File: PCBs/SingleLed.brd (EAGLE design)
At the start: 11.1 x 29.2 mm, 4 parts

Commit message: Updated
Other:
- board size 11.1 x 29.2 mm -> 15 x 28.7 mm
- board text added: "PinwheelRobotics"
- board text added: "care@pinwheel.in"
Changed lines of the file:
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@@
 <setting verticaltext="up"/>
 </settings>
-<grid distance="50" unitdist="mil" unit="mm" style="lines" multiple="1" display="yes" altdistance="5" altunitdist="mil" altunit="mm"/>
+<grid distance="0.5" unitdist="mm" unit="mm" style="lines" multiple="1" display="yes" altdistance="5" altunitdist="mil" altunit="mm"/>
 <layers>
 <layer number="1" name="Top" color="4" fill="1" visible="yes" active="yes"/>
@@
 <layer number="43" name="vRestrict" color="2" fill="10" visible="yes" active="yes"/>
 <layer number="44" name="Drills" color="7" fill="1" visible="no" active="yes"/>
-<layer number="45" name="Holes" color="7" fill="1" visible="no" active="yes"/>
+<layer number="45" name="Holes" color="7" fill="1" visible="yes" active="yes"/>
 <layer number="46" name="Milling" color="3" fill="1" visible="no" active="yes"/>
 <layer number="47" name="Measures" color="7" fill="1" visible="no" active="yes"/>
@@
 <board>
 <plain>
-<wire x1="17.78" y1="13.97" x2="28.88" y2="13.97" width="0" layer="20"/>
-<wire x1="28.88" y1="13.97" x2="28.88" y2="43.17" width="0" layer="20"/>
-<wire x1="28.88" y1="43.17" x2="17.78" y2="43.17" width="0" layer="20"/>
-<wire x1="17.78" y1="43.17" x2="17.78" y2="13.97" width="0" layer="20"/>
+<wire x1="14.95735625" y1="41.5157875" x2="14.998034375" y2="14.995496875" width="0" layer="20"/>
+<wire x1="14.998034375" y1="14.995496875" x2="16.28164375" y2="13.714" width="0" layer="20" curve="89.911983"/>
+<wire x1="16.28164375" y1="13.714" x2="28.00465625" y2="13.714" width="0" layer="20"/>
+<wire x1="28.00465625" y1="13.714" x2="30" y2="15.70934375" width="0" layer="20" curve="90"/>
+<wire x1="30" y1="15.70934375" x2="30" y2="41.302534375" width="0" layer="20"/>
+<wire x1="30" y1="41.302534375" x2="28.902534375" y2="42.4" width="0" layer="20" curve="90"/>
+<wire x1="28.902534375" y1="42.4" x2="15.84123125" y2="42.4" width="0" layer="20"/>
+<wire x1="15.84123125" y1="42.4" x2="14.95735625" y2="41.5157875" width="0" layer="20" curve="90.021878"/>
+<hole x="17.018" y="40.386" drill="3"/>
+<hole x="17.018" y="16.002" drill="3"/>
+<hole x="27.94" y="16.002" drill="3"/>
+<hole x="27.94" y="40.513" drill="3"/>
+<text x="17.272" y="17.653" size="1.778" layer="21" rot="R90">PinwheelRobotics</text>
+<text x="29.718" y="37.465" size="1.778" layer="22" rot="MR270">care@pinwheel.in</text>
 </plain>
 <attributes>
@@
 </element>
 <element name="U$2" library="microbit" package="MICROBIT_PAD" value="MICROBIT_PAD" x="22.479" y="35.306" smashed="yes" rot="R180">
-<attribute name="NAME" x="26.035" y="41.529" size="1.27" layer="21" rot="R270"/>
+<attribute name="NAME" x="17.653" y="36.449" size="1.27" layer="21" rot="R270"/>
 </element>
 <element name="R1" library="adafruit" package="0204/7" value="" x="26.67" y="31.75" smashed="yes" rot="R270">

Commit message: New Update
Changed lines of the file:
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@@
 <drawing>
 <settings>
-<setting alwaysvectorfont="yes"/>
+<setting alwaysvectorfont="no"/>
 <setting verticaltext="up"/>
 </settings>
@@
 <wire x1="28.902534375" y1="42.4" x2="15.84123125" y2="42.4" width="0" layer="20"/>
 <wire x1="15.84123125" y1="42.4" x2="14.95735625" y2="41.5157875" width="0" layer="20" curve="90.021878"/>
-<hole x="17.018" y="40.386" drill="3"/>
-<hole x="17.018" y="16.002" drill="3"/>
-<hole x="27.94" y="16.002" drill="3"/>
-<hole x="27.94" y="40.513" drill="3"/>
+<hole x="17" y="40.5" drill="3"/>
+<hole x="17" y="16" drill="3"/>
+<hole x="28" y="16" drill="3"/>
+<hole x="28" y="40.5" drill="3"/>
 <text x="17.272" y="17.653" size="1.778" layer="21" rot="R90">PinwheelRobotics</text>
 <text x="29.718" y="37.465" size="1.778" layer="22" rot="MR270">care@pinwheel.in</text>

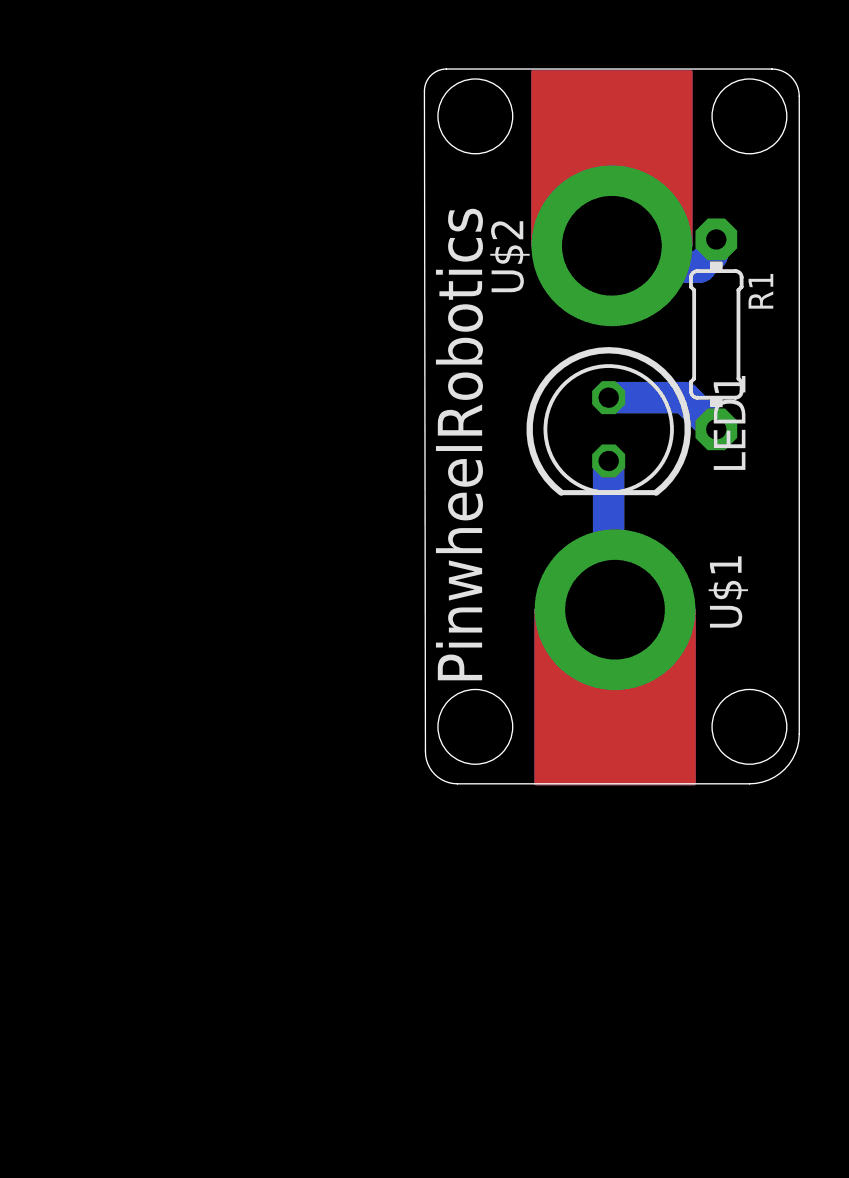
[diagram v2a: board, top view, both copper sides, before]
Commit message: New Update for board curv
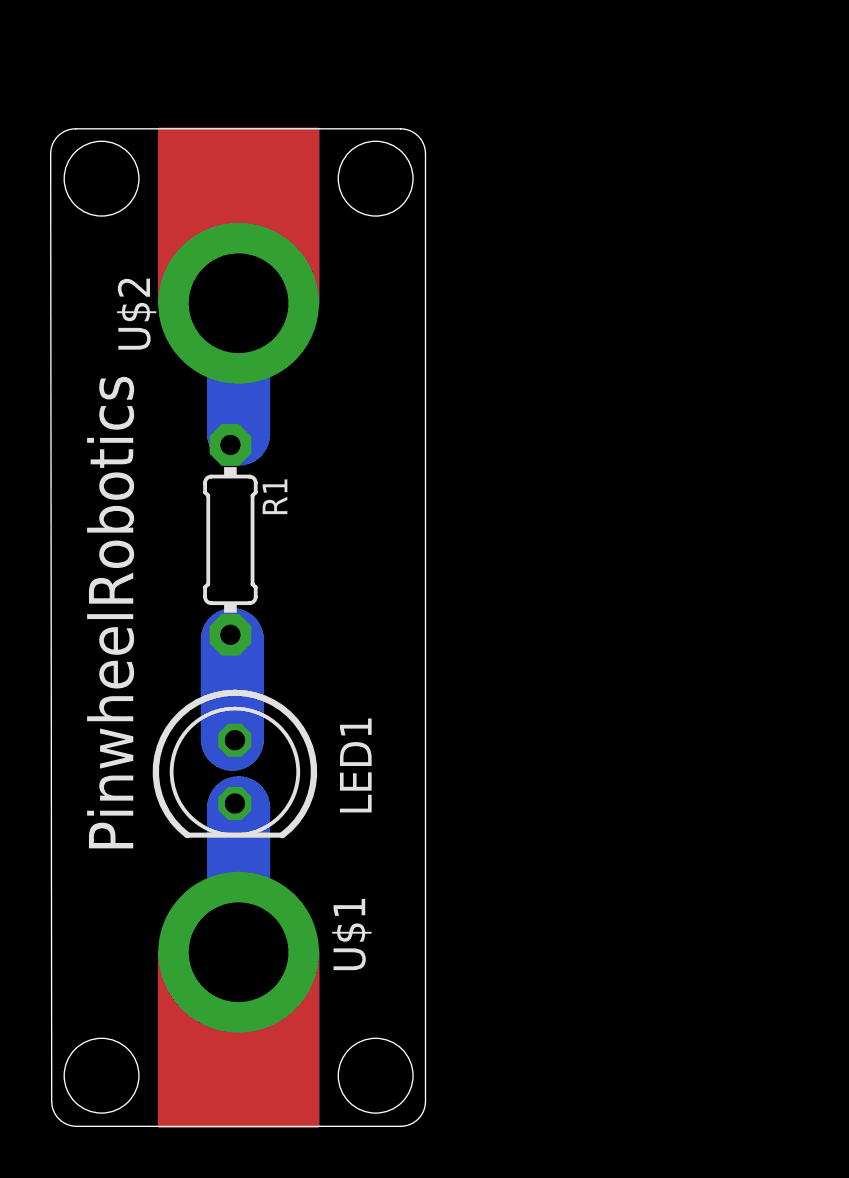
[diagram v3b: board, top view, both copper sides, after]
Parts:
- moved R1 21.2 mm to (7.17, 23.5)
- moved U$1 20.4 mm to (7.50, 6.96)
- moved LED1 20.3 mm to (7.35, 14.2)
- moved U$2 15.2 mm to (7.50, 33.0)
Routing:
- net N$3: track 5.26 -> 5.81 mm
- net N$1: track 4.84 -> 4.32 mm
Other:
- board size 15 x 28.7 mm -> 15 x 40 mm
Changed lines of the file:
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@@
 <drawing>
 <settings>
-<setting alwaysvectorfont="no"/>
+<setting alwaysvectorfont="yes"/>
 <setting verticaltext="up"/>
 </settings>
@@
 <board>
 <plain>
-<wire x1="14.95735625" y1="41.5157875" x2="14.998034375" y2="14.995496875" width="0" layer="20"/>
-<wire x1="14.998034375" y1="14.995496875" x2="16.28164375" y2="13.714" width="0" layer="20" curve="89.911983"/>
-<wire x1="16.28164375" y1="13.714" x2="28.00465625" y2="13.714" width="0" layer="20"/>
-<wire x1="28.00465625" y1="13.714" x2="30" y2="15.70934375" width="0" layer="20" curve="90"/>
-<wire x1="30" y1="15.70934375" x2="30" y2="41.302534375" width="0" layer="20"/>
-<wire x1="30" y1="41.302534375" x2="28.902534375" y2="42.4" width="0" layer="20" curve="90"/>
-<wire x1="28.902534375" y1="42.4" x2="15.84123125" y2="42.4" width="0" layer="20"/>
-<wire x1="15.84123125" y1="42.4" x2="14.95735625" y2="41.5157875" width="0" layer="20" curve="90.021878"/>
-<hole x="17" y="40.5" drill="3"/>
-<hole x="17" y="16" drill="3"/>
-<hole x="28" y="16" drill="3"/>
-<hole x="28" y="40.5" drill="3"/>
-<text x="17.272" y="17.653" size="1.778" layer="21" rot="R90">PinwheelRobotics</text>
-<text x="29.718" y="37.465" size="1.778" layer="22" rot="MR270">care@pinwheel.in</text>
+<wire x1="-0.0429" y1="38.9992" x2="-0.001096875" y2="0.96595625" width="0" layer="20"/>
+<wire x1="-0.001096875" y1="0.96595625" x2="0.9989" y2="-0.032" width="0" layer="20" curve="89.936795"/>
+<wire x1="0.9989" y1="-0.032" x2="14" y2="-0.032" width="0" layer="20"/>
+<wire x1="14" y1="-0.032" x2="15" y2="0.968" width="0" layer="20" curve="90"/>
+<wire x1="15" y1="0.968" x2="15" y2="39" width="0" layer="20"/>
+<wire x1="15" y1="39" x2="14" y2="40" width="0" layer="20" curve="90"/>
+<wire x1="14" y1="40" x2="0.9571" y2="40" width="0" layer="20"/>
+<wire x1="0.9571" y1="40" x2="-0.0429" y2="38.9992" width="0" layer="20" curve="90.045837"/>
+<hole x="2" y="38" drill="3"/>
+<hole x="2" y="2" drill="3"/>
+<hole x="13" y="2" drill="3"/>
+<hole x="13" y="38" drill="3"/>
+<text x="3.272" y="10.907" size="1.778" layer="21" rot="R90">PinwheelRobotics</text>
+<text x="13.218" y="31.219" size="1.778" layer="22" rot="MR270">care@pinwheel.in</text>
 </plain>
 <attributes>
@@
 </autorouter>
 <elements>
-<element name="LED1" library="led" library_urn="urn:adsk.eagle:library:259" package="LED5MM" package3d_urn="urn:adsk.eagle:package:15799/2" value="" x="22.352" y="27.94" smashed="yes" rot="R270">
-<attribute name="NAME" x="26.5684" y="30.226" size="1.27" layer="25" ratio="10" rot="R270"/>
-<attribute name="POPULARITY" value="93" x="-13.208" y="6.35" size="1.778" layer="27" rot="R270" display="off"/>
-<attribute name="VALUE" x="20.5486" y="24.7396" size="1.27" layer="27" ratio="10" rot="R270"/>
+<element name="LED1" library="led" library_urn="urn:adsk.eagle:library:259" package="LED5MM" package3d_urn="urn:adsk.eagle:package:15799/2" value="" x="7.352" y="14.194" smashed="yes" rot="R270">
+<attribute name="NAME" x="11.5684" y="16.48" size="1.27" layer="25" ratio="10" rot="R270"/>
+<attribute name="POPULARITY" value="93" x="-28.208" y="-7.396" size="1.778" layer="27" rot="R270" display="off"/>
+<attribute name="VALUE" x="5.5486" y="10.9936" size="1.27" layer="27" ratio="10" rot="R270"/>
 </element>
-<element name="U$1" library="microbit" package="MICROBIT_PAD" value="MICROBIT_PAD" x="22.606" y="20.701" smashed="yes">
-<attribute name="NAME" x="26.416" y="22.987" size="1.27" layer="21" rot="R270"/>
+<element name="U$1" library="microbit" package="MICROBIT_PAD" value="MICROBIT_PAD" x="7.5" y="6.955" smashed="yes">
+<attribute name="NAME" x="11.31" y="9.241" size="1.27" layer="21" rot="R270"/>
 </element>
-<element name="U$2" library="microbit" package="MICROBIT_PAD" value="MICROBIT_PAD" x="22.479" y="35.306" smashed="yes" rot="R180">
-<attribute name="NAME" x="17.653" y="36.449" size="1.27" layer="21" rot="R270"/>
+<element name="U$2" library="microbit" package="MICROBIT_PAD" value="MICROBIT_PAD" x="7.5" y="33" smashed="yes" rot="R180">
+<attribute name="NAME" x="2.674" y="34.143" size="1.27" layer="21" rot="R270"/>
 </element>
-<element name="R1" library="adafruit" package="0204/7" value="" x="26.67" y="31.75" smashed="yes" rot="R270">
-<attribute name="NAME" x="27.9654" y="34.29" size="0.9906" layer="25" ratio="12" rot="R270"/>
-<attribute name="VALUE" x="26.1874" y="33.3756" size="0.9906" layer="27" ratio="12" rot="R270"/>
+<element name="R1" library="adafruit" package="0204/7" value="" x="7.17" y="23.504" smashed="yes" rot="R270">
+<attribute name="NAME" x="8.4654" y="26.044" size="0.9906" layer="25" ratio="12" rot="R270"/>
+<attribute name="VALUE" x="6.6874" y="25.1296" size="0.9906" layer="27" ratio="12" rot="R270"/>
 </element>
 </elements>
@@
 <contactref element="U$1" pad="PAD"/>
 <contactref element="LED1" pad="K"/>
-<wire x1="22.4028" y1="20.8788" x2="22.5552" y2="20.7264" width="0.1524" layer="16"/>
-<wire x1="22.4028" y1="26.67" x2="22.352" y2="26.67" width="0.1524" layer="16"/>
-<wire x1="22.5552" y1="20.7264" x2="22.606" y2="20.701" width="0.1524" layer="16"/>
-<wire x1="22.352" y1="26.67" x2="22.352" y2="20.9296" width="1.27" layer="16"/>
-<wire x1="22.352" y1="20.9296" x2="22.4028" y2="20.8788" width="1.27" layer="16"/>
+<wire x1="7.5" y1="6.955" x2="7.5" y2="12.75" width="2.54" layer="16"/>
+<wire x1="7.5" y1="12.75" x2="7.352" y2="12.924" width="0.1524" layer="16"/>
 </signal>
 <signal name="N$1">
 <contactref element="LED1" pad="A"/>
 <contactref element="R1" pad="2"/>
-<wire x1="22.352" y1="29.21" x2="25.4" y2="29.21" width="1.27" layer="16"/>
-<wire x1="25.4" y1="29.21" x2="26.67" y2="27.94" width="1.27" layer="16"/>
+<wire x1="7.25" y1="19.5" x2="7.25" y2="15.5" width="2.54" layer="16"/>
+<wire x1="7.25" y1="15.5" x2="7.352" y2="15.464" width="0.1524" layer="16"/>
+<wire x1="7.25" y1="19.5" x2="7.17" y2="19.694" width="0.1524" layer="16"/>
 </signal>
 <signal name="N$3">
 <contactref element="U$2" pad="PAD"/>
 <contactref element="R1" pad="1"/>
-<wire x1="26.5049" y1="34.95354375" x2="26.00645625" y2="34.4551" width="1.27" layer="16"/>
-<wire x1="26.00645625" y1="34.4551" x2="25.17454375" y2="34.4551" width="1.27" layer="16"/>
-<wire x1="26.67" y1="35.56" x2="26.5049" y2="35.3949" width="1.27" layer="16"/>
-<wire x1="26.5049" y1="35.3949" x2="26.5049" y2="34.95354375" width="1.27" layer="16"/>
-<wire x1="25.17454375" y1="34.4551" x2="24.32364375" y2="35.306" width="1.27" layer="16"/>
-<wire x1="24.32364375" y1="35.306" x2="22.479" y2="35.306" width="1.27" layer="16"/>
+<wire x1="7.5" y1="27.75" x2="7.25" y2="27.5" width="0.1524" layer="16"/>
+<wire x1="7.5" y1="33" x2="7.5" y2="27.75" width="2.54" layer="16"/>
+<wire x1="7.25" y1="27.5" x2="7.17" y2="27.314" width="0.1524" layer="16"/>
 </signal>
 </signals>

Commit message: Dimension added
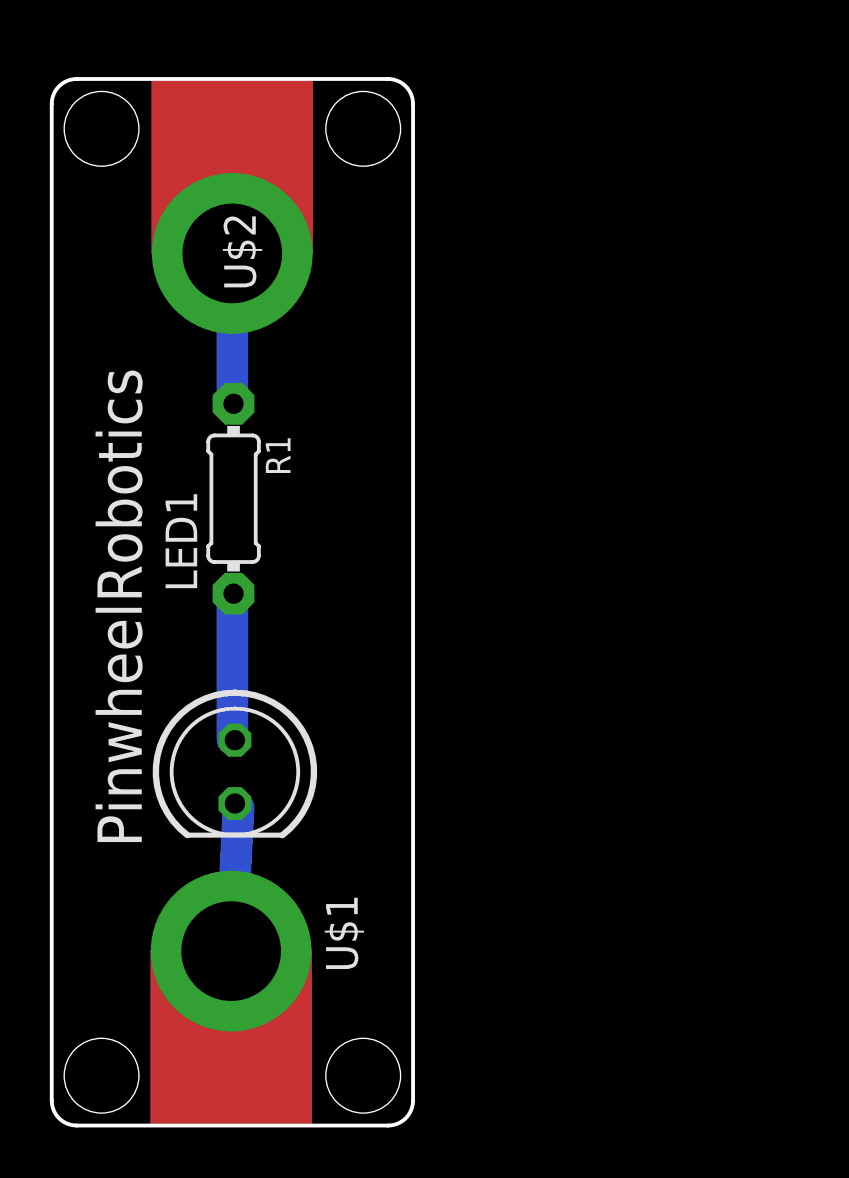
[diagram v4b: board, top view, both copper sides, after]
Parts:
- moved U$2 2.02 mm to (7.25, 35.0)
- moved R1 1.66 mm to (7.30, 25.2)
- moved U$1 0.30 mm to (7.20, 7.00)
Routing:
- net N$1: track 4.32 -> 5.96 mm
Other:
- board size 15 x 40 mm -> 14.5 x 42 mm
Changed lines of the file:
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@@
 <board>
 <plain>
-<wire x1="-0.0429" y1="38.9992" x2="-0.001096875" y2="0.96595625" width="0" layer="20"/>
-<wire x1="-0.001096875" y1="0.96595625" x2="0.9989" y2="-0.032" width="0" layer="20" curve="89.936795"/>
-<wire x1="0.9989" y1="-0.032" x2="14" y2="-0.032" width="0" layer="20"/>
-<wire x1="14" y1="-0.032" x2="15" y2="0.968" width="0" layer="20" curve="90"/>
-<wire x1="15" y1="0.968" x2="15" y2="39" width="0" layer="20"/>
-<wire x1="15" y1="39" x2="14" y2="40" width="0" layer="20" curve="90"/>
-<wire x1="14" y1="40" x2="0.9571" y2="40" width="0" layer="20"/>
-<wire x1="0.9571" y1="40" x2="-0.0429" y2="38.9992" width="0" layer="20" curve="90.045837"/>
-<hole x="2" y="38" drill="3"/>
+<hole x="2" y="40" drill="3"/>
 <hole x="2" y="2" drill="3"/>
-<hole x="13" y="2" drill="3"/>
-<hole x="13" y="38" drill="3"/>
-<text x="3.272" y="10.907" size="1.778" layer="21" rot="R90">PinwheelRobotics</text>
-<text x="13.218" y="31.219" size="1.778" layer="22" rot="MR270">care@pinwheel.in</text>
+<hole x="12.5" y="2" drill="3"/>
+<hole x="12.5" y="40" drill="3"/>
+<text x="3.613" y="11.161" size="1.778" layer="21" rot="R90">PinwheelRobotics</text>
+<text x="13.242" y="30.965" size="1.778" layer="22" rot="MR270">care@pinwheel.in</text>
+<wire x1="1" y1="0" x2="13.5" y2="0" width="0.1524" layer="20"/>
+<wire x1="13.5" y1="0" x2="14.5" y2="1" width="0.1524" layer="20" curve="90"/>
+<wire x1="14.5" y1="1" x2="14.5" y2="41" width="0.1524" layer="20"/>
+<wire x1="14.5" y1="41" x2="13.5" y2="42" width="0.1524" layer="20" curve="90"/>
+<wire x1="13.5" y1="42" x2="1" y2="42" width="0.1524" layer="20"/>
+<wire x1="1" y1="42" x2="0" y2="41" width="0.1524" layer="20" curve="90"/>
+<wire x1="0" y1="41" x2="0" y2="1" width="0.1524" layer="20"/>
+<wire x1="0" y1="1" x2="1" y2="0" width="0.1524" layer="20" curve="90"/>
 </plain>
 <attributes>
@@
 <elements>
 <element name="LED1" library="led" library_urn="urn:adsk.eagle:library:259" package="LED5MM" package3d_urn="urn:adsk.eagle:package:15799/2" value="" x="7.352" y="14.194" smashed="yes" rot="R270">
-<attribute name="NAME" x="11.5684" y="16.48" size="1.27" layer="25" ratio="10" rot="R270"/>
+<attribute name="NAME" x="4.5684" y="25.48" size="1.27" layer="25" ratio="10" rot="R270"/>
 <attribute name="POPULARITY" value="93" x="-28.208" y="-7.396" size="1.778" layer="27" rot="R270" display="off"/>
 <attribute name="VALUE" x="5.5486" y="10.9936" size="1.27" layer="27" ratio="10" rot="R270"/>
 </element>
-<element name="U$1" library="microbit" package="MICROBIT_PAD" value="MICROBIT_PAD" x="7.5" y="6.955" smashed="yes">
-<attribute name="NAME" x="11.31" y="9.241" size="1.27" layer="21" rot="R270"/>
-</element>
-<element name="U$2" library="microbit" package="MICROBIT_PAD" value="MICROBIT_PAD" x="7.5" y="33" smashed="yes" rot="R180">
-<attribute name="NAME" x="2.674" y="34.143" size="1.27" layer="21" rot="R270"/>
-</element>
-<element name="R1" library="adafruit" package="0204/7" value="" x="7.17" y="23.504" smashed="yes" rot="R270">
-<attribute name="NAME" x="8.4654" y="26.044" size="0.9906" layer="25" ratio="12" rot="R270"/>
-<attribute name="VALUE" x="6.6874" y="25.1296" size="0.9906" layer="27" ratio="12" rot="R270"/>
+<element name="U$1" library="microbit" package="MICROBIT_PAD" value="MICROBIT_PAD" x="7.2" y="7" smashed="yes">
+<attribute name="NAME" x="11.01" y="9.286" size="1.27" layer="21" rot="R270"/>
+</element>
+<element name="U$2" library="microbit" package="MICROBIT_PAD" value="MICROBIT_PAD" x="7.246" y="35" smashed="yes" rot="R180">
+<attribute name="NAME" x="6.92" y="36.643" size="1.27" layer="21" rot="R270"/>
+</element>
+<element name="R1" library="adafruit" package="0204/7" value="" x="7.297" y="25.155" smashed="yes" rot="R270">
+<attribute name="NAME" x="8.5924" y="27.695" size="0.9906" layer="25" ratio="12" rot="R270"/>
+<attribute name="VALUE" x="6.8144" y="26.7806" size="0.9906" layer="27" ratio="12" rot="R270"/>
 </element>
 </elements>
@@
 <contactref element="U$1" pad="PAD"/>
 <contactref element="LED1" pad="K"/>
-<wire x1="7.5" y1="6.955" x2="7.5" y2="12.75" width="2.54" layer="16"/>
+<wire x1="7.2" y1="7" x2="7.5" y2="12.75" width="1.27" layer="16"/>
 <wire x1="7.5" y1="12.75" x2="7.352" y2="12.924" width="0.1524" layer="16"/>
 </signal>
@@
 <contactref element="LED1" pad="A"/>
 <contactref element="R1" pad="2"/>
-<wire x1="7.25" y1="19.5" x2="7.25" y2="15.5" width="2.54" layer="16"/>
+<wire x1="7.25" y1="21.231025" x2="7.25" y2="15.5" width="1.27" layer="16"/>
 <wire x1="7.25" y1="15.5" x2="7.352" y2="15.464" width="0.1524" layer="16"/>
-<wire x1="7.25" y1="19.5" x2="7.17" y2="19.694" width="0.1524" layer="16"/>
+<wire x1="7.25" y1="21.231025" x2="7.297" y2="21.345" width="0.1524" layer="16"/>
 </signal>
 <signal name="N$3">
 <contactref element="U$2" pad="PAD"/>
 <contactref element="R1" pad="1"/>
-<wire x1="7.5" y1="27.75" x2="7.25" y2="27.5" width="0.1524" layer="16"/>
-<wire x1="7.5" y1="33" x2="7.5" y2="27.75" width="2.54" layer="16"/>
-<wire x1="7.25" y1="27.5" x2="7.17" y2="27.314" width="0.1524" layer="16"/>
+<wire x1="7.246" y1="35" x2="7.246" y2="29.083575" width="1.27" layer="16"/>
+<wire x1="7.246" y1="29.083575" x2="7.297" y2="28.965" width="0.1524" layer="16"/>
 </signal>
 </signals>
